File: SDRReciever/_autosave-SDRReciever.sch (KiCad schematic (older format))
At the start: 80 parts, among them J1 Conn_Coaxial, J10 I_0, J11 I_180, J12 Q_90, J13 Q_270, J14 I_OUT, J15 Q_OUT, J16 5V, J17 4.3V, J18 Conn_01x02_Female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

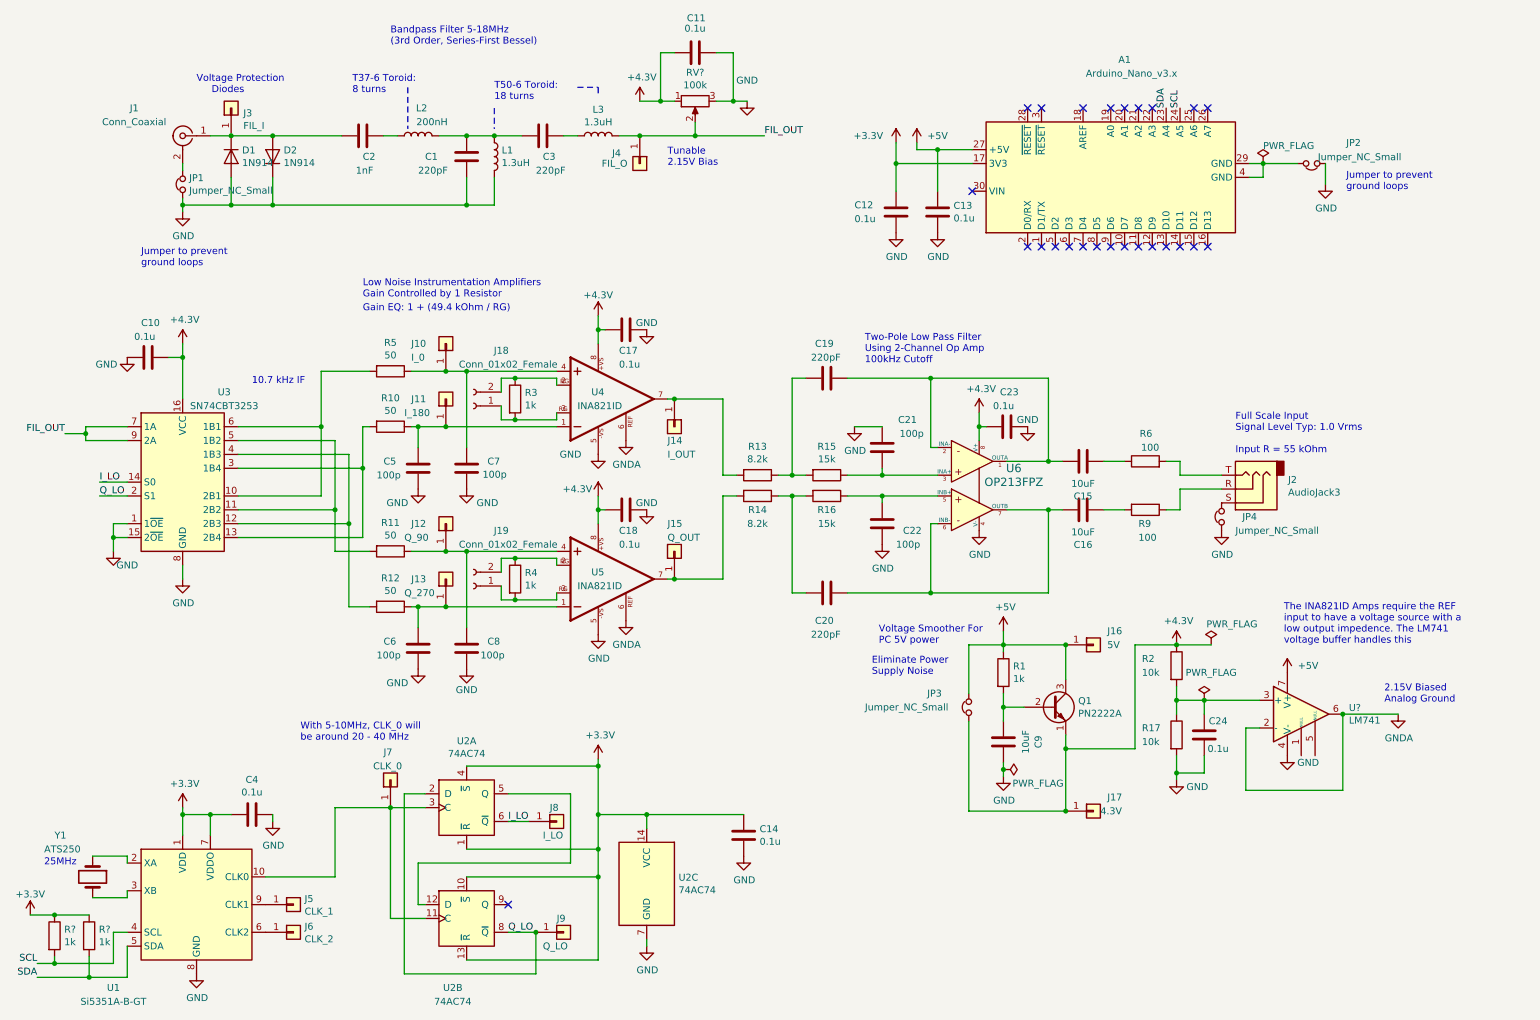
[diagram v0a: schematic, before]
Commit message: Added ltspice sims, revision document, image of the prototype, made some changes to the schematic (i believe just the title block)
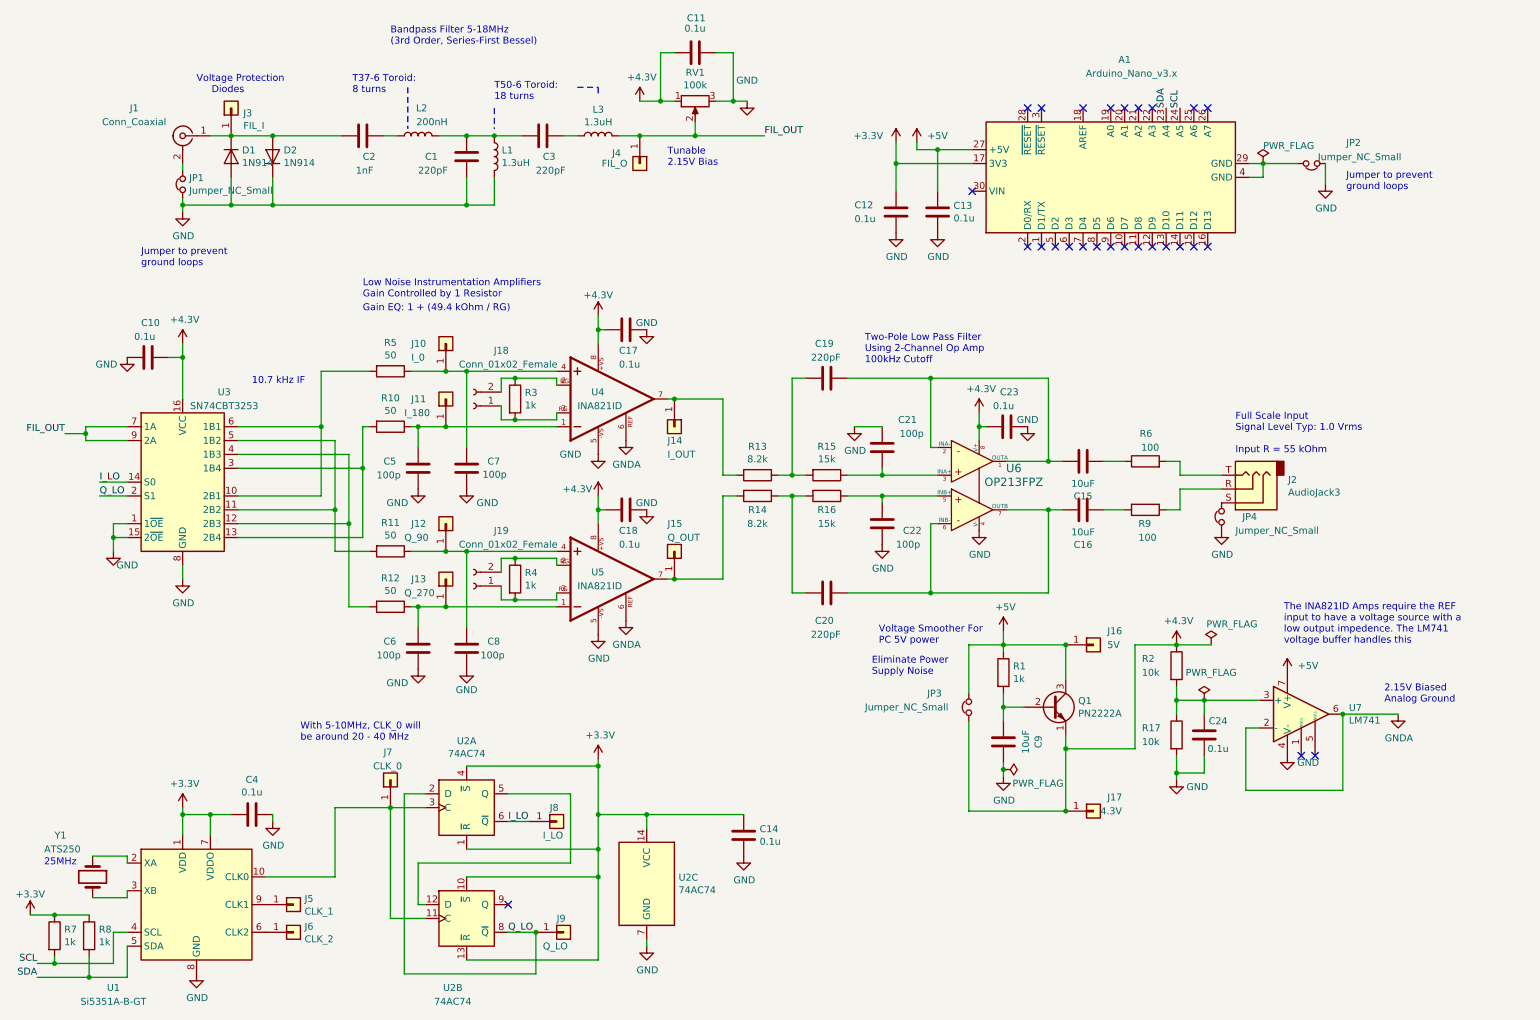
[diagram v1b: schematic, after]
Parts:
- gave numbers to parts that had none: 4
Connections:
- no-connect marks 25 -> 27
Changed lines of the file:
@@
 Sheet 1 1
 Title "Low(ish) Cost SDR Reciever"
-Date "2020-04-17"
+Date "2020-06-04"
 Rev "3"
 Comp "Walla Walla University"
-Comment1 ""
+Comment1 "Partner: Caleb Froelich"
 Comment2 ""
 Comment3 "ENGR 357"
@@
 	3450 4850 3650 4850
 $Comp
-L Amplifier_Operational:LM741 U?
+L Amplifier_Operational:LM741 U7
 U 1 1 5EDAB873
 P 9825 5625
-F 0 "U?" H 10169 5671 50  0000 L CNN
+F 0 "U7" H 10169 5671 50  0000 L CNN
 F 1 "LM741" H 10169 5580 50  0000 L CNN
 F 2 "" H 9875 5675 50  0001 C CNN
@@
 $EndComp
 $Comp
-L power:+5V #PWR?
+L power:+5V #PWR042
 U 1 1 5EDC9E45
 P 9725 5325
-F 0 "#PWR?" H 9725 5175 50  0001 C CNN
+F 0 "#PWR042" H 9725 5175 50  0001 C CNN
 F 1 "+5V" H 9875 5375 50  0000 C CNN
 F 2 "" H 9725 5325 50  0001 C CNN
@@
 	10125 6175 10125 5625
 $Comp
-L power:GND #PWR?
+L power:GND #PWR026
 U 1 1 5EDF4DF4
 P 8925 6100
-F 0 "#PWR?" H 8925 5850 50  0001 C CNN
+F 0 "#PWR026" H 8925 5850 50  0001 C CNN
 F 1 "GND" H 9075 6050 50  0000 C CNN
 F 2 "" H 8925 6100 50  0001 C CNN
@@
 The INA821ID Amps require the REF\ninput to have a voltage source with a\nlow output impedence. The LM741\nvoltage buffer handles this
 $Comp
-L Device:R_POT RV?
+L Device:R_POT RV1
 U 1 1 5EE830FE
 P 5450 1200
-F 0 "RV?" V 5243 1200 50  0000 C CNN
+F 0 "RV1" V 5243 1200 50  0000 C CNN
 F 1 "100k" V 5334 1200 50  0000 C CNN
 F 2 "" H 5450 1200 50  0001 C CNN
@@
 	700  7525 1075 7525
 $Comp
-L Device:R R?
+L Device:R R7
 U 1 1 5EF8A4E5
 P 825 7225
-F 0 "R?" H 895 7271 50  0000 L CNN
+F 0 "R7" H 895 7271 50  0000 L CNN
 F 1 "1k" H 895 7180 50  0000 L CNN
 F 2 "" V 755 7225 50  0001 C CNN
@@
 $EndComp
 $Comp
-L Device:R R?
+L Device:R R8
 U 1 1 5EF8B556
 P 1075 7225
-F 0 "R?" H 1145 7271 50  0000 L CNN
+F 0 "R8" H 1145 7271 50  0000 L CNN
 F 1 "1k" H 1145 7180 50  0000 L CNN
 F 2 "" V 1005 7225 50  0001 C CNN
@@
 	1075 7525 1075 7375
 $Comp
-L power:+3.3V #PWR?
+L power:+3.3V #PWR025
 U 1 1 5EFAA0AC
 P 650 7075
-F 0 "#PWR?" H 650 6925 50  0001 C CNN
+F 0 "#PWR025" H 650 6925 50  0001 C CNN
 F 1 "+3.3V" H 650 7225 50  0000 C CNN
 F 2 "" H 650 7075 50  0001 C CNN
@@
 Text Notes 750  6725 0    50   ~ 0
 25MHz
+NoConn ~ 9825 5925
+NoConn ~ 9925 5925
 $EndSCHEMATC
